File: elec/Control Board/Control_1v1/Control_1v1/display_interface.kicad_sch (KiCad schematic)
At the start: 4 parts, among them J35 Conn_02x05_Odd_Even, J36 Conn_02x05_Odd_Even

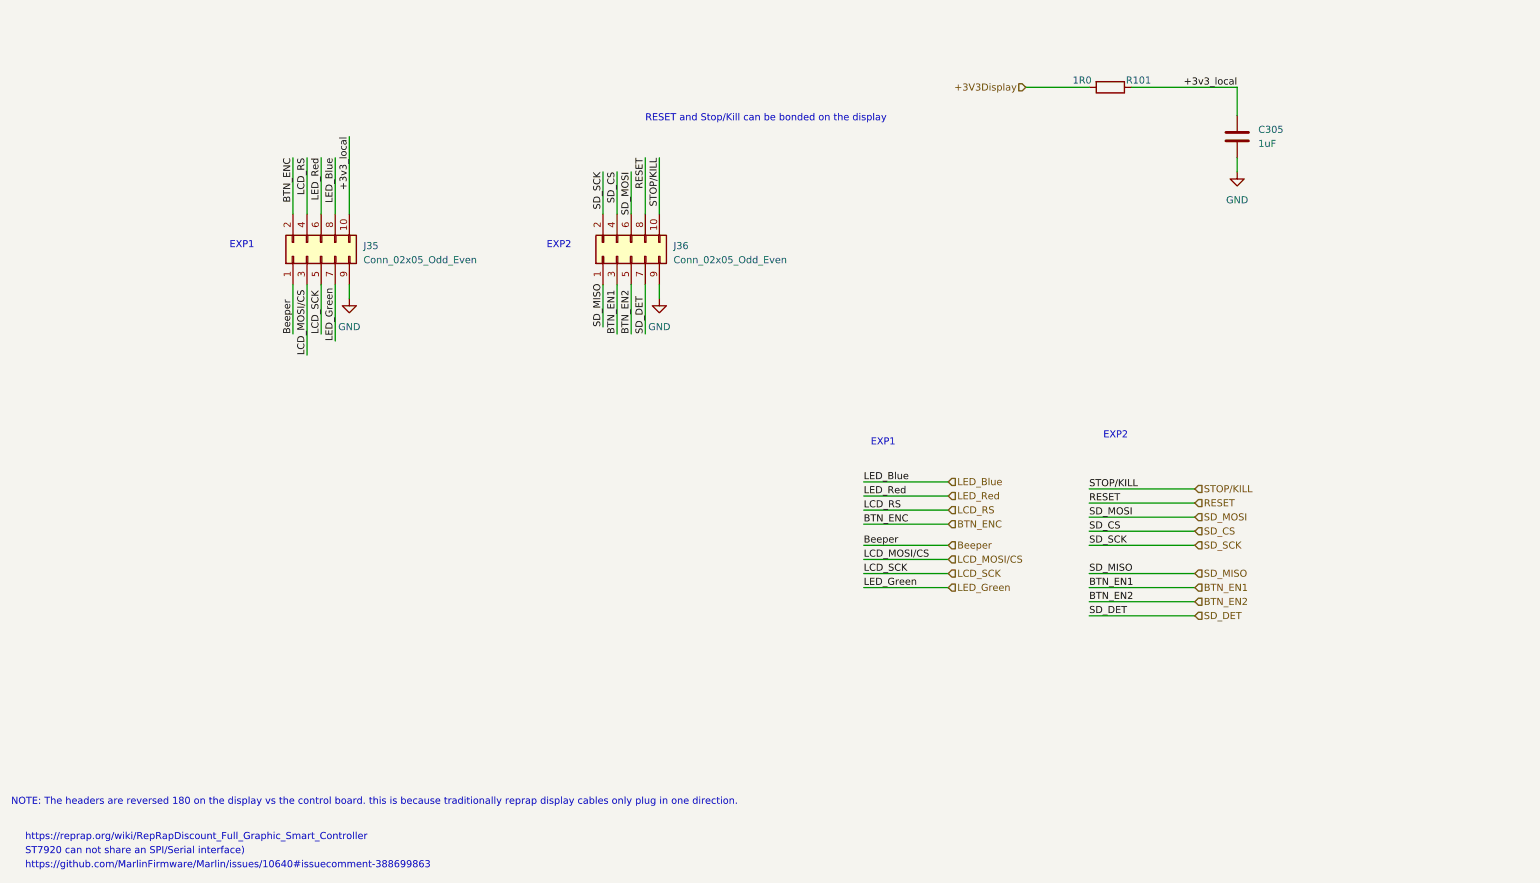
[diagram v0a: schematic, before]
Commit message: Update schematic to reflect some reworks to V1.1 assemblies. 5V to Display. Display signal names. J35 pin8 to 10 short.
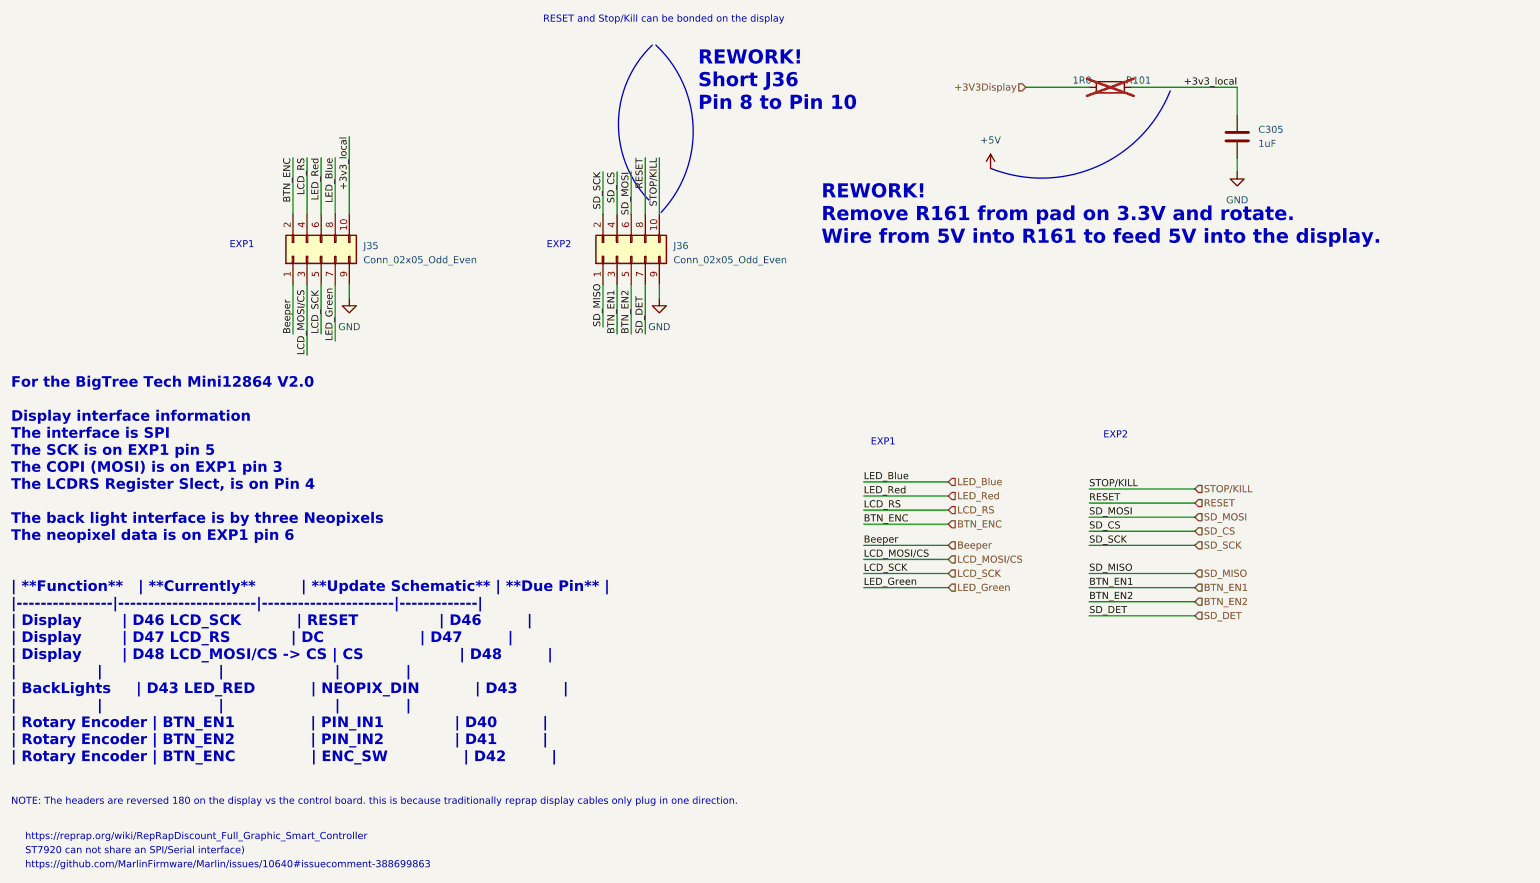
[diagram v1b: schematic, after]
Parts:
- R101: now not fitted
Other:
- note added: "For the BigTree Tech Mini12864 V2.0 Display interface information The interface is SPI The SCK is on EXP1 pin 5 The COPI (MOSI) is on EXP1 pin 3 The LCDRS Register Slect, is on Pin 4 The back light interface is by three Neopixels The neopixel data is on EXP1 pin 6 | **Function** | **Currently** | **Update Schematic** | **Due Pin** | |----------------|-----------------------|----------------------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"
- note added: "REWORK! Remove R161 from pad on 3.3V and rotate. Wire from 5V into R161 to feed 5V into the display."
- note added: "REWORK! Short J36 Pin 8 to Pin 10"
- title: Control Interconnect Board OEDCS -> Control Interconnect Board OEDCS With Reworks
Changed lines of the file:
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@@
   (paper "A4")
   (title_block
-    (title "Control Interconnect Board OEDCS")
-    (date "2023-10-10")
+    (title "Control Interconnect Board OEDCS With Reworks")
+    (date "2023-12-06")
     (rev "Rev 1.1")
     (company "Public Invention")
@@
     (stroke (width 0) (type default))
   )
-  (text "RESET and Stop/Kill can be bonded on the display" (at 137.16 34.29 0)
+  (arc (start 137.795 48.26) (mid 132.3259 34.1585) (end 138.43 20.32)
+    (stroke (width 0) (type default))
+    (fill (type none))
+  )
+  (arc (start 231.775 28.575) (mid 218.4758 42.2672) (end 199.39 42.545)
+    (stroke (width 0) (type default))
+    (fill (type none))
+  )
+  (arc (start 139.065 20.32) (mid 145.7873 35.2038) (end 140.017 50.482)
+    (stroke (width 0) (type default))
+    (fill (type none))
+  )
+  (text "RESET and Stop/Kill can be bonded on the display" (at 118.745 16.51 0)
     (effects (font (size 1.27 1.27)) (justify left bottom))
   )
@@
     (effects (font (size 1.27 1.27)) (justify left bottom))
   )
+  (text "For the BigTree Tech Mini12864 V2.0\n\nDisplay interface information\nThe interface is SPI\nThe SCK is on EXP1 pin 5\nThe COPI (MOSI) is on EXP1 pin 3\nThe LCDRS Register Slect, is on Pin 4\n\nThe back light interface is by three Neopixels\nThe neopixel data is on EXP1 pin 6\n\n\n| **Function**   | **Currently**         | **Update Schematic** | **Due Pin** |\n|----------------|-----------------------|----------------------|-------------|\n| Display        | D46 LCD_SCK           | RESET                | D46         |\n| Display        | D47 LCD_RS            | DC                   | D47         |\n| Display        | D48 LCD_MOSI/CS -> CS | CS                   | D48         |\n|                |                       |                      |             |\n| BackLights     | D43 LED_RED           | NEOPIX_DIN           | D43         |\n|                |                       |                      |             |\n| Rotary Encoder | BTN_EN1               | PIN_IN1              | D40         |\n| Rotary Encoder | BTN_EN2               | PIN_IN2              | D41         |\n| Rotary Encoder | BTN_ENC               | ENC_SW               | D42         |"
+    (at 22.86 149.86 0)
+    (effects (font (face "Courier New") (size 1.905 1.905) (thickness 0.381) bold) (justify left bottom))
+  )
+  (text "REWORK!\nShort J36\nPin 8 to Pin 10" (at 146.685 32.385 0)
+    (effects (font (size 2.54 2.54) (thickness 0.508) bold) (justify left bottom))
+  )
   (text "EXP1\n" (at 177.8 92.71 0)
     (effects (font (size 1.27 1.27)) (justify left bottom))
@@
   (text "EXP1\n" (at 62.23 57.15 0)
     (effects (font (size 1.27 1.27)) (justify left bottom))
+  )
+  (text "REWORK!\nRemove R161 from pad on 3.3V and rotate. \nWire from 5V into R161 to feed 5V into the display."
+    (at 168.91 56.515 0)
+    (effects (font (size 2.54 2.54) (thickness 0.508) bold) (justify left bottom))
   )
   (text "ST7920 can not share an SPI/Serial interface)" (at 25.4 166.37 0)
@@
     )
   )
+  (symbol (lib_id "power:+5V") (at 199.39 42.545 0) (unit 1)
+    (in_bom yes) (on_board yes) (dnp no) (fields_autoplaced)
+    (property "Reference" "#PWR025" (at 199.39 46.355 0)
+      (effects (font (size 1.27 1.27)) hide)
+    )
+    (property "Value" "+5V" (at 199.39 37.465 0)
+      (effects (font (size 1.27 1.27)))
+    )
+    (property "Footprint" "" (at 199.39 42.545 0)
+      (effects (font (size 1.27 1.27)) hide)
+    )
+    (property "Datasheet" "" (at 199.39 42.545 0)
+      (effects (font (size 1.27 1.27)) hide)
+    )
+    (pin "1")
+    (instances
+      (project "Control_1v1"
+        (path "/c68c9deb-8d4d-42f0-adf8-4d3022f4ee59"
+          (reference "#PWR025") (unit 1)
+        )
+        (path "/c68c9deb-8d4d-42f0-adf8-4d3022f4ee59/f2cc20dc-f81b-4e9e-a9e1-88ed6ea8264c"
+          (reference "#PWR0108") (unit 1)
+        )
+      )
+    )
+  )
   (symbol (lib_id "Connector_Generic:Conn_02x05_Odd_Even") (at 78.74 58.42 90) (unit 1)
     (in_bom yes) (on_board yes) (dnp no) (fields_autoplaced)
@@
   )
   (symbol (lib_id "Device:R") (at 220.98 27.94 270) (unit 1)
-    (in_bom yes) (on_board yes) (dnp no)
+    (in_bom yes) (on_board yes) (dnp yes)
     (property "Reference" "R101" (at 226.06 26.67 90)
       (effects (font (size 1.27 1.27)))
